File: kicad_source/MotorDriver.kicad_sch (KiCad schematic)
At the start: 53 parts, among them P10 WR-TBL_691313710002, P7 WR-TBL_691322310002, P8 WR-TBL_691313710002, P9 WR-TBL_691313710002, Q1 2N7002, Q2 IPD90P03P4L- 04, U4 74xx08, U5 IFX007T, U6 IFX007T, U7 IFX007T, U8 IFX007T

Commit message: updated layout
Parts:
- C10, C12, C8: footprint capacitors:C_elec_THT_16x25_RM7.5 -> Capacitor_THT:CP_Radial_D16.0mm_P7.50mm
- C11, C9: footprint capacitors:TantalC_SizeD_EIA-7343_Wave -> Capacitor_Tantalum_SMD:CP_EIA-7343-15_Kemet-W
- C13, C14, C15, C16, C17, C18, C19, C20, C21, C22, C23, C24, C25, C26, C27, C28, C29, C30, C7: footprint capacitors:C_0603 -> Capacitor_SMD:C_0603_1608Metric
- D4, D5: footprint diodes:SOD-123 -> Diode_SMD:D_SOD-123
- R10, R11, R12, R13, R14, R15, R16, R17, R18, R19, R20, R21, R22, R23, R24: footprint resistors:R_0603 -> Resistor_SMD:R_0603_1608Metric
- U4: footprint SOIC:SOIC-14_3.9x8.7mm_Pitch1.27mm -> Package_SO:SOIC-14_3.9x8.7mm_P1.27mm
- U5, U6, U7, U8: footprint SOT_TO:TO-263-7Lead -> Package_TO_SOT_SMD:TO-263-7_TabPin8

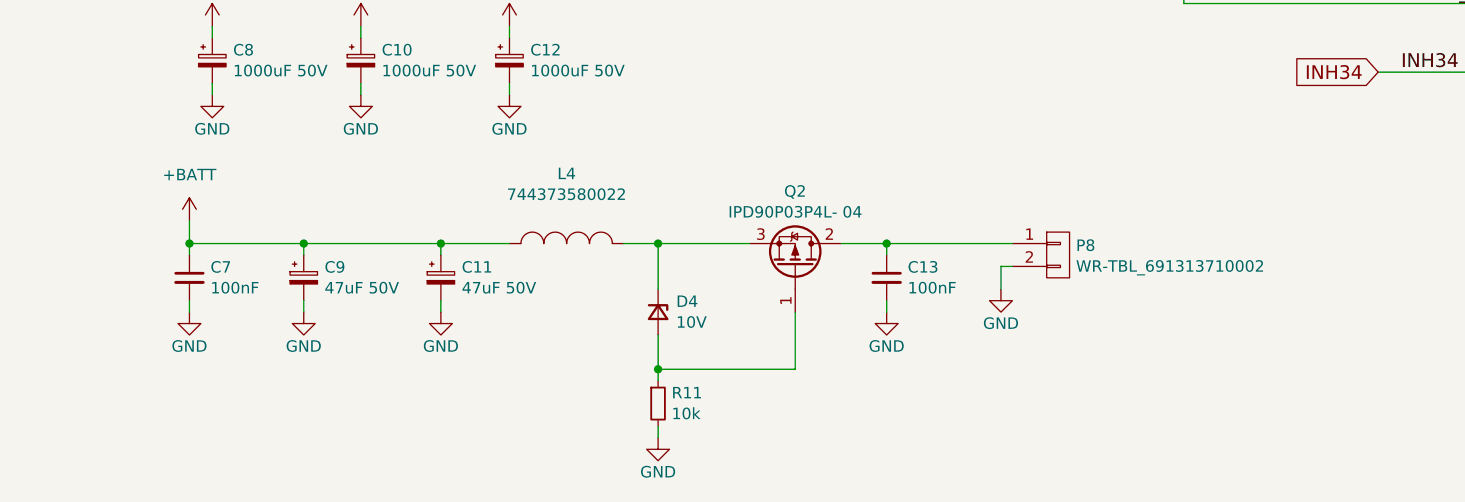
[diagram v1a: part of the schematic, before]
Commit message: moved input circuit to voltage regulator side
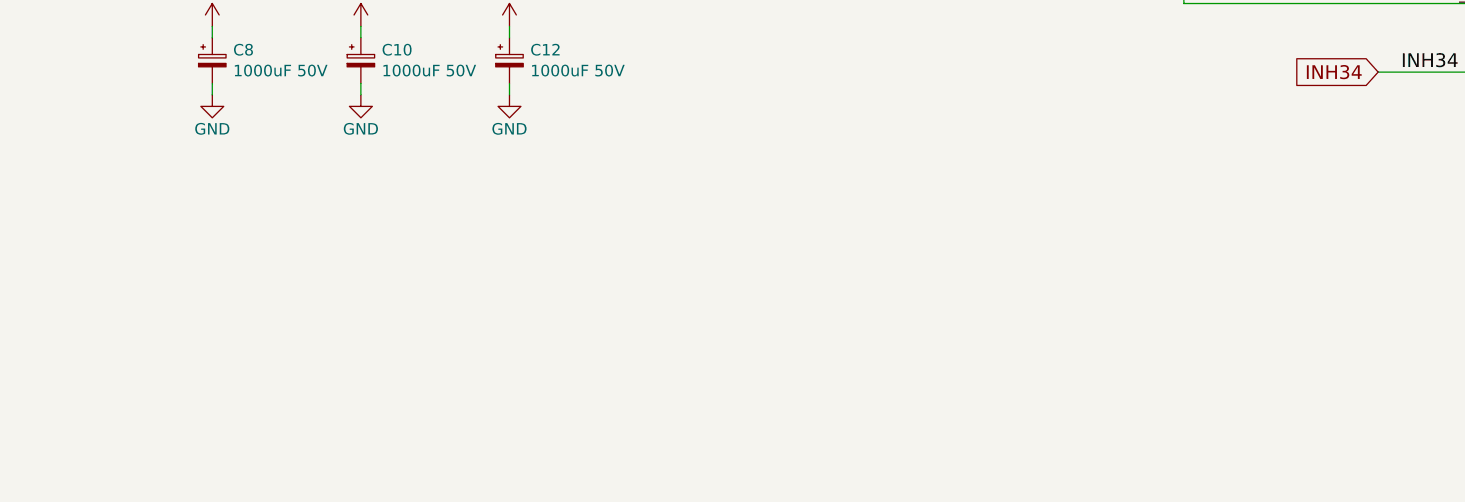
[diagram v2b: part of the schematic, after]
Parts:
- removed C11, C9: 47uF 50V, Capacitor_Tantalum_SMD:CP_EIA-7343-15_Kemet-W, symbol Device:C_Polarized_Small
- removed C13, C7: 100nF, Capacitor_SMD:C_0603_1608Metric, symbol Device:C_Small
- removed D4: 10V, Diode_SMD:D_SOD-123, symbol Device:D_Zener_Small
- removed L4: 744373580022, L_power:WE-LHMI80xx, symbol OpenCyphalRobotController07-rescue:74437346082-L_power
- removed P8: WR-TBL_691313710002, CON_wuerth:WR-TBL_691313710002, symbol OpenCyphalRobotController07-rescue:WR-TBL_691313710002-mechanical-connectors
- removed Q2: IPD90P03P4L- 04, SOT_TO:TO-252-2Lead, symbol Device:Q_PMOS_GDS
- removed R11: 10k, Resistor_SMD:R_0603_1608Metric, symbol Device:R_Small

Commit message: added page with outputs
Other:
- title: OpenCyphalRobotController07 -> CyphalRobotController07/CAN
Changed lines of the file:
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@@
   (paper "A4")
   (title_block
-    (title "OpenCyphalRobotController07")
-    (date "2023-07-24")
+    (title "CyphalRobotController07/CAN")
+    (date "2023-10-01")
     (rev "0.1")
     (company "generationmake")

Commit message: started layout
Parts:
- renumbered C14 to C10, C15 to C11, C16 to C12, C17 to C13, C18 to C14, C19 to C15, C20 to C16, C21 to C17, C22 to C18, C23 to C19, C24 to C20, C25 to C21, C26 to C22, C27 to C23, C28 to C24, C29 to C25, C30 to C26, C8 to C7, C10 to C8, C12 to C9, D5 to D4, P7 to J7, P9 to J8, P10 to J9, R12 to R11, R13 to R12, R14 to R13, R15 to R14, R16 to R15, R17 to R16, R18 to R17, R19 to R18, R20 to R19, R21 to R20, R22 to R21, R23 to R22, R24 to R23

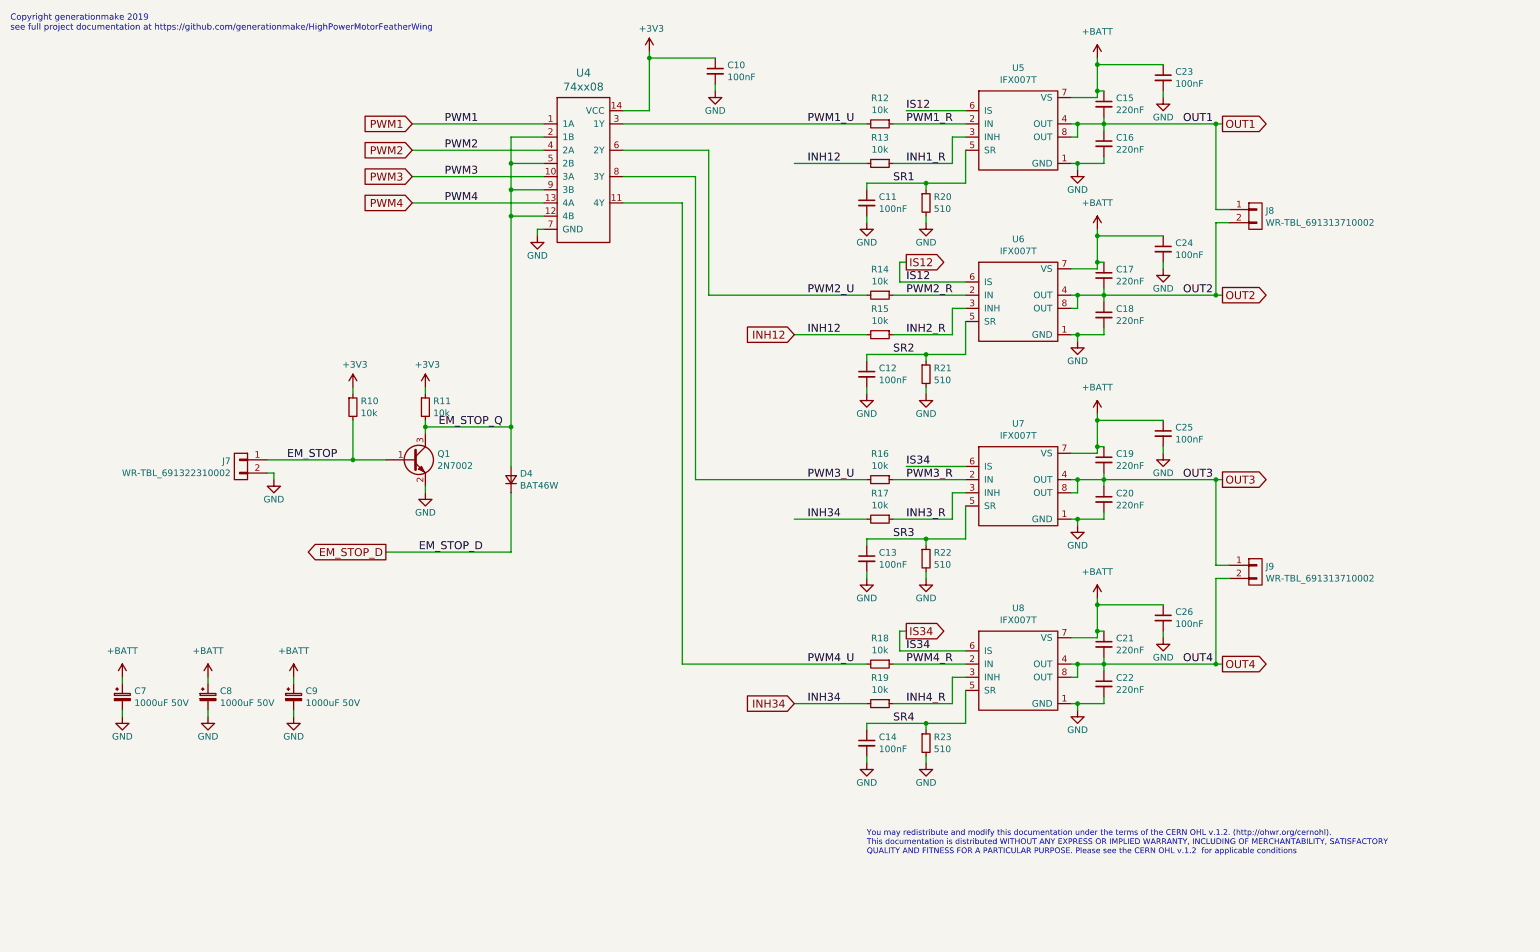
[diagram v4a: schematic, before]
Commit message: made first draft of placement
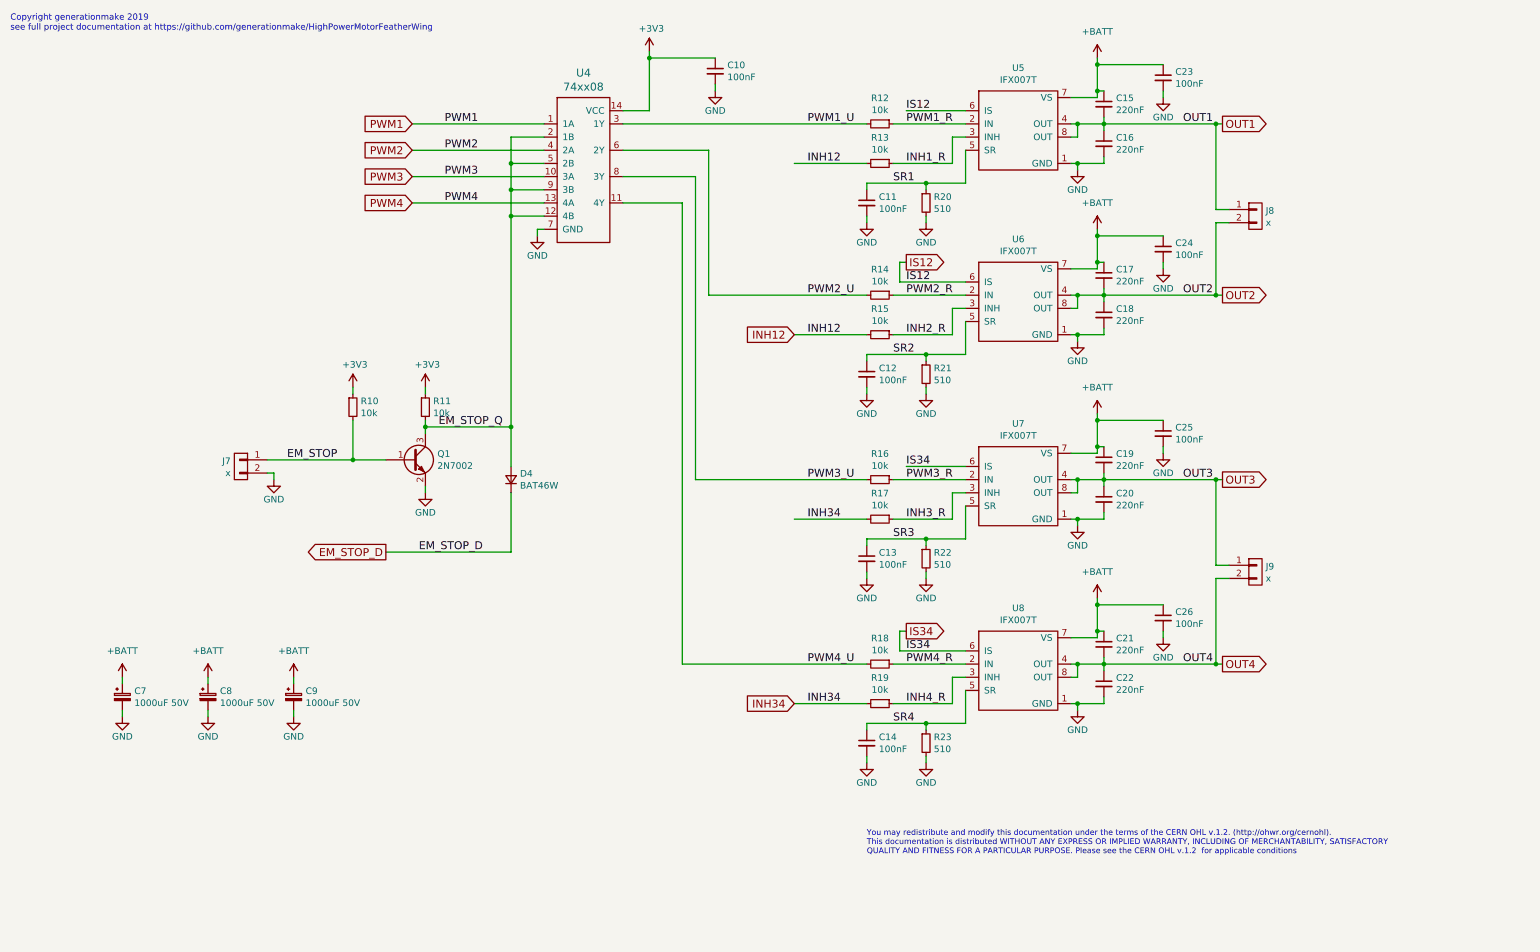
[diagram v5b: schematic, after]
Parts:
- J7: value WR-TBL_691322310002 -> x; footprint CON_wuerth:WR-TBL_691322310002 -> Connector_Phoenix_MC:PhoenixContact_MCV_1,5_2-G-3.81_1x02_P3.81mm_Vertical
- J8, J9: value WR-TBL_691313710002 -> x; footprint CON_wuerth:WR-TBL_691313710002 -> Connector_Phoenix_MC:PhoenixContact_MCV_1,5_2-G-3.81_1x02_P3.81mm_Vertical
- Q1: footprint SOT_TO:SOT-23 -> Package_TO_SOT_SMD:SOT-23
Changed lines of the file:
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@@
       (effects (font (size 1.27 1.27)) (justify left))
     )
-    (property "Value" "WR-TBL_691313710002" (id 1) (at 254.7112 53.34 0)
-      (effects (font (size 1.27 1.27)) (justify left))
-    )
-    (property "Footprint" "CON_wuerth:WR-TBL_691313710002" (id 2) (at 250.19 50.8 0)
+    (property "Value" "x" (id 1) (at 254.7112 53.34 0)
+      (effects (font (size 1.27 1.27)) (justify left))
+    )
+    (property "Footprint" "Connector_Phoenix_MC:PhoenixContact_MCV_1,5_2-G-3.81_1x02_P3.81mm_Vertical" (id 2) (at 250.19 50.8 0)
       (effects (font (size 1.27 1.27)) hide)
     )
@@
       (effects (font (size 1.27 1.27)) (justify left))
     )
-    (property "Value" "WR-TBL_691313710002" (id 1) (at 254.7112 121.92 0)
-      (effects (font (size 1.27 1.27)) (justify left))
-    )
-    (property "Footprint" "CON_wuerth:WR-TBL_691313710002" (id 2) (at 250.19 119.38 0)
+    (property "Value" "x" (id 1) (at 254.7112 121.92 0)
+      (effects (font (size 1.27 1.27)) (justify left))
+    )
+    (property "Footprint" "Connector_Phoenix_MC:PhoenixContact_MCV_1,5_2-G-3.81_1x02_P3.81mm_Vertical" (id 2) (at 250.19 119.38 0)
       (effects (font (size 1.27 1.27)) hide)
     )
@@
       (effects (font (size 1.27 1.27)) (justify left))
     )
-    (property "Footprint" "SOT_TO:SOT-23" (id 2) (at 95.25 96.52 0)
+    (property "Footprint" "Package_TO_SOT_SMD:SOT-23" (id 2) (at 95.25 96.52 0)
       (effects (font (size 1.27 1.27)) hide)
     )
@@
       (effects (font (size 1.27 1.27)) (justify left))
     )
-    (property "Value" "WR-TBL_691322310002" (id 1) (at 55.1688 101.6 0)
-      (effects (font (size 1.27 1.27)) (justify left))
-    )
-    (property "Footprint" "CON_wuerth:WR-TBL_691322310002" (id 2) (at 59.69 99.06 0)
-      (effects (font (size 1.27 1.27)) hide)
-    )
+    (property "Value" "x" (id 1) (at 55.1688 101.6 0)
+      (effects (font (size 1.27 1.27)) (justify left))
+    )
+    (property "Footprint" "Connector_Phoenix_MC:PhoenixContact_MCV_1,5_2-G-3.81_1x02_P3.81mm_Vertical" (id 2) (at 59.69 99.06 0)
+      (effects (font (size 1.27 1.27)) hide)
+    )

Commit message: made first draft of layout
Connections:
- net OUT1: now also J8.2 (P2); no longer J8.1 (P1)
- net OUT2: now also J8.1 (P1); no longer J8.2 (P2)
- net OUT3: now also J9.2 (P2); no longer J9.1 (P1)
- net OUT4: now also J9.1 (P1); no longer J9.2 (P2)
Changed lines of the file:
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@@
     )
   )
-  (symbol (lib_id "OpenCyphalRobotController07-rescue:WR-TBL_691313710002-mechanical-connectors") (at 252.73 52.07 0) (unit 1)
+  (symbol (lib_id "OpenCyphalRobotController07-rescue:WR-TBL_691313710002-mechanical-connectors") (at 252.73 52.07 0) (mirror x) (unit 1)
     (in_bom yes) (on_board yes)
-    (property "Reference" "J8" (id 0) (at 254.7112 51.0286 0)
+    (property "Reference" "J8" (id 0) (at 254.7112 53.1114 0)
       (effects (font (size 1.27 1.27)) (justify left))
     )
-    (property "Value" "x" (id 1) (at 254.7112 53.34 0)
+    (property "Value" "x" (id 1) (at 254.7112 50.8 0)
       (effects (font (size 1.27 1.27)) (justify left))
     )
-    (property "Footprint" "Connector_Phoenix_MC:PhoenixContact_MCV_1,5_2-G-3.81_1x02_P3.81mm_Vertical" (id 2) (at 250.19 50.8 0)
+    (property "Footprint" "Connector_Phoenix_MC:PhoenixContact_MCV_1,5_2-G-3.81_1x02_P3.81mm_Vertical" (id 2) (at 250.19 53.34 0)
       (effects (font (size 1.27 1.27)) hide)
     )
@@
     (pin "2")
   )
-  (symbol (lib_id "OpenCyphalRobotController07-rescue:WR-TBL_691313710002-mechanical-connectors") (at 252.73 120.65 0) (unit 1)
+  (symbol (lib_id "OpenCyphalRobotController07-rescue:WR-TBL_691313710002-mechanical-connectors") (at 252.73 120.65 0) (mirror x) (unit 1)
     (in_bom yes) (on_board yes)
-    (property "Reference" "J9" (id 0) (at 254.7112 119.6086 0)
+    (property "Reference" "J9" (id 0) (at 254.7112 121.6914 0)
       (effects (font (size 1.27 1.27)) (justify left))
     )
-    (property "Value" "x" (id 1) (at 254.7112 121.92 0)
+    (property "Value" "x" (id 1) (at 254.7112 119.38 0)
       (effects (font (size 1.27 1.27)) (justify left))
     )
-    (property "Footprint" "Connector_Phoenix_MC:PhoenixContact_MCV_1,5_2-G-3.81_1x02_P3.81mm_Vertical" (id 2) (at 250.19 119.38 0)
+    (property "Footprint" "Connector_Phoenix_MC:PhoenixContact_MCV_1,5_2-G-3.81_1x02_P3.81mm_Vertical" (id 2) (at 250.19 121.92 0)
       (effects (font (size 1.27 1.27)) hide)
     )
